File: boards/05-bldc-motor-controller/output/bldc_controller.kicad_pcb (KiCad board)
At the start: 2 copper layers, 80 x 100 mm, 55 parts, among them J1 Power Input, J2 Motor Output, J3 Hall Sensors, J4 SWD-6, Q1 IRLZ44N, Q2 IRLZ44N, Q3 IRLZ44N, Q4 IRLZ44N, Q5 IRLZ44N, Q6 IRLZ44N, U1 LM2596-5.0, U10 STM32G431K8Tx, U2 AMS1117-3.3, U3 DRV8301, Y1 8MHz

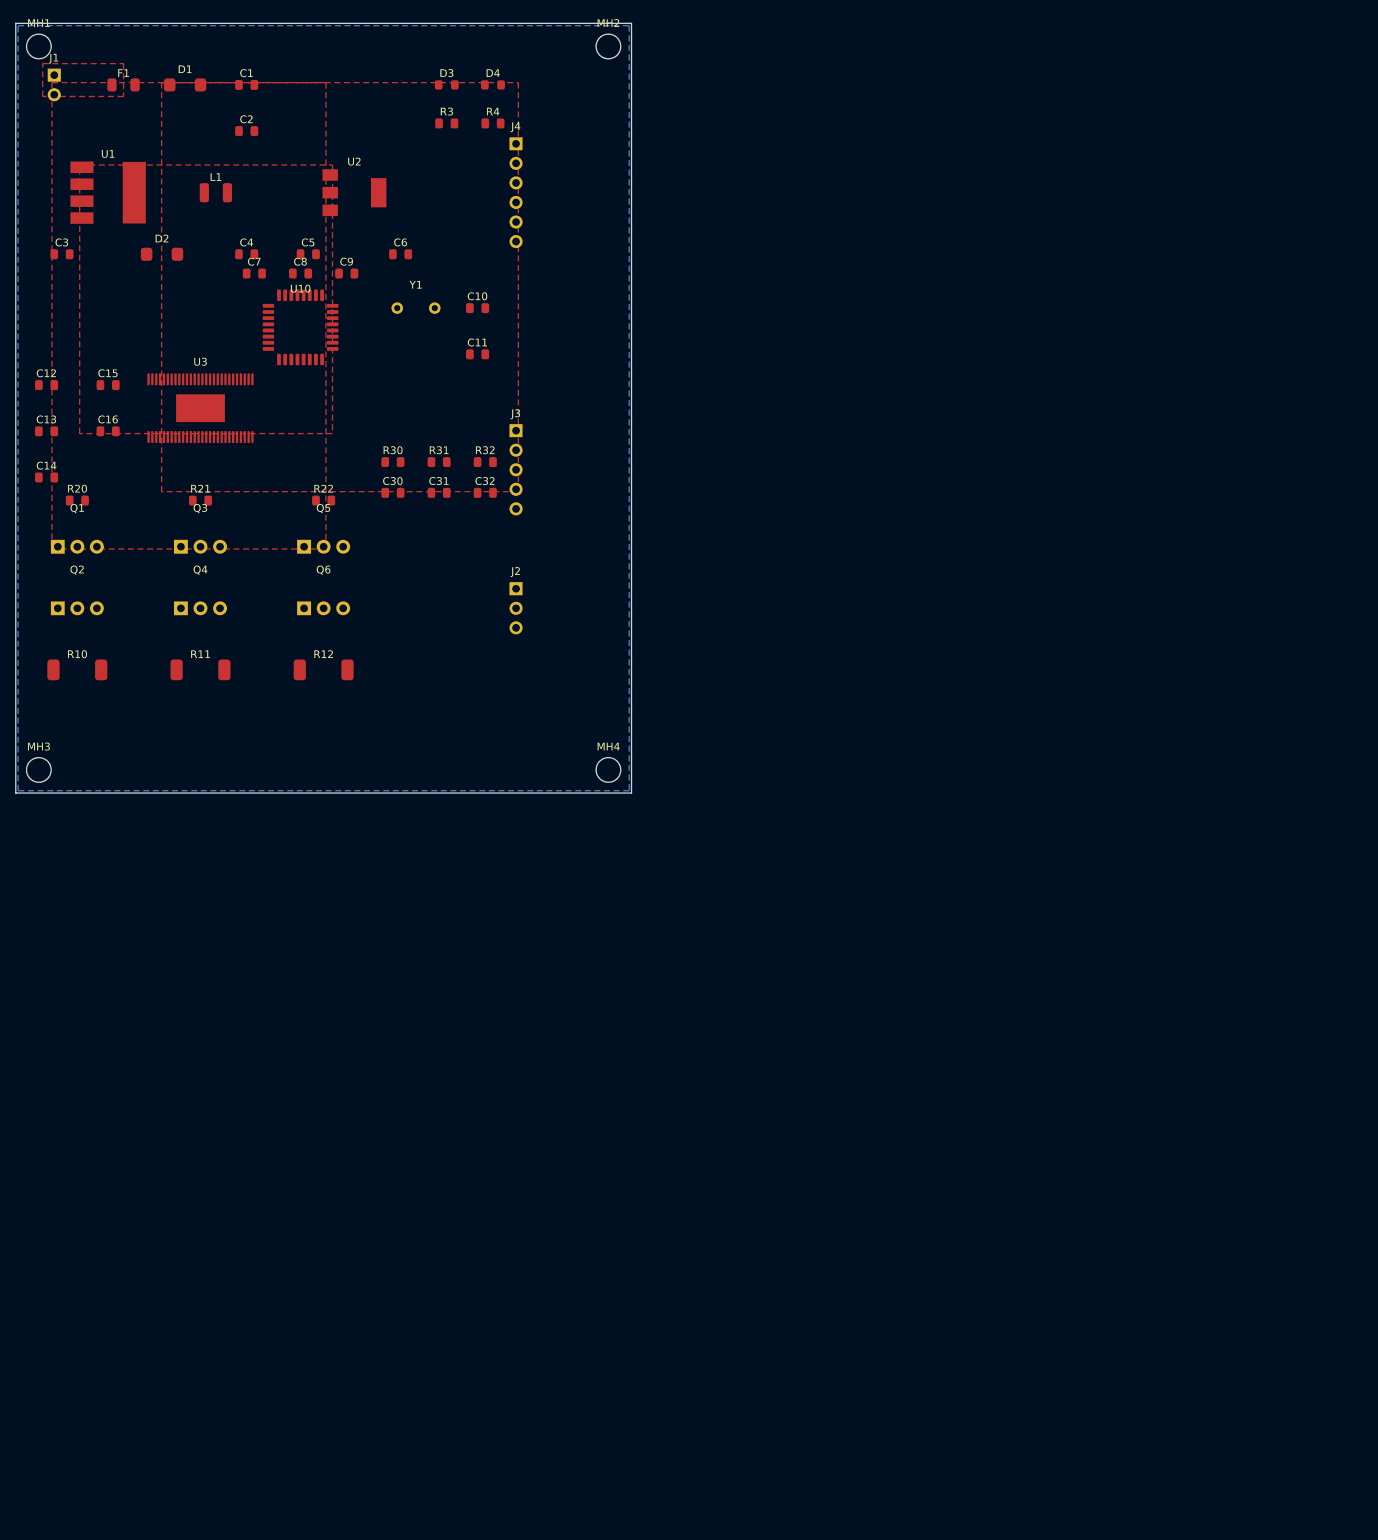
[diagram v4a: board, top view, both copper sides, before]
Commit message: fix(pcb): page-fit routed boards only; revert unrouted sources (refs #3714)
page_fit was applied to and committed for the UNROUTED board sources too.
Because the autorouter is absolute-grid-position-dependent, translating the
unrouted boards changed routing outcomes and turned CI red on three jobs:
- Test: board-02 re-route produced a platform-specific segment count.
- Diff-Pair (06) / Match-Group (07): re-routing the moved unrouted boards
  fractured plane nets under the copper-union pour audit (#3509/#3617).

page_fit is a pure post-route translation, so it must touch the ROUTED
output only:
- Revert every unrouted boards/*/output/<name>.kicad_pcb to origin/main
  (byte-identical); keep the page-fitted *_routed.kicad_pcb (gallery/viewer).
- Revert tests/router/test_board02_manufacturable_baseline.py to main
  (unrouted board-02 unchanged -> reproduces main's result).
- Build hook: _run_step_page_fit now operates on the routed PCB only and
  skips cleanly when no routed output exists, instead of falling back to and
  persisting a page-fit unrouted PCB.

Retains the sound geometry fixes (translation-invariant
point_to_segment_distance, _format_coord_mm, diffpair +1e-6 window tolerance).

Co-Authored-By: Claude Opus 4.7 <noreply@anthropic.com>
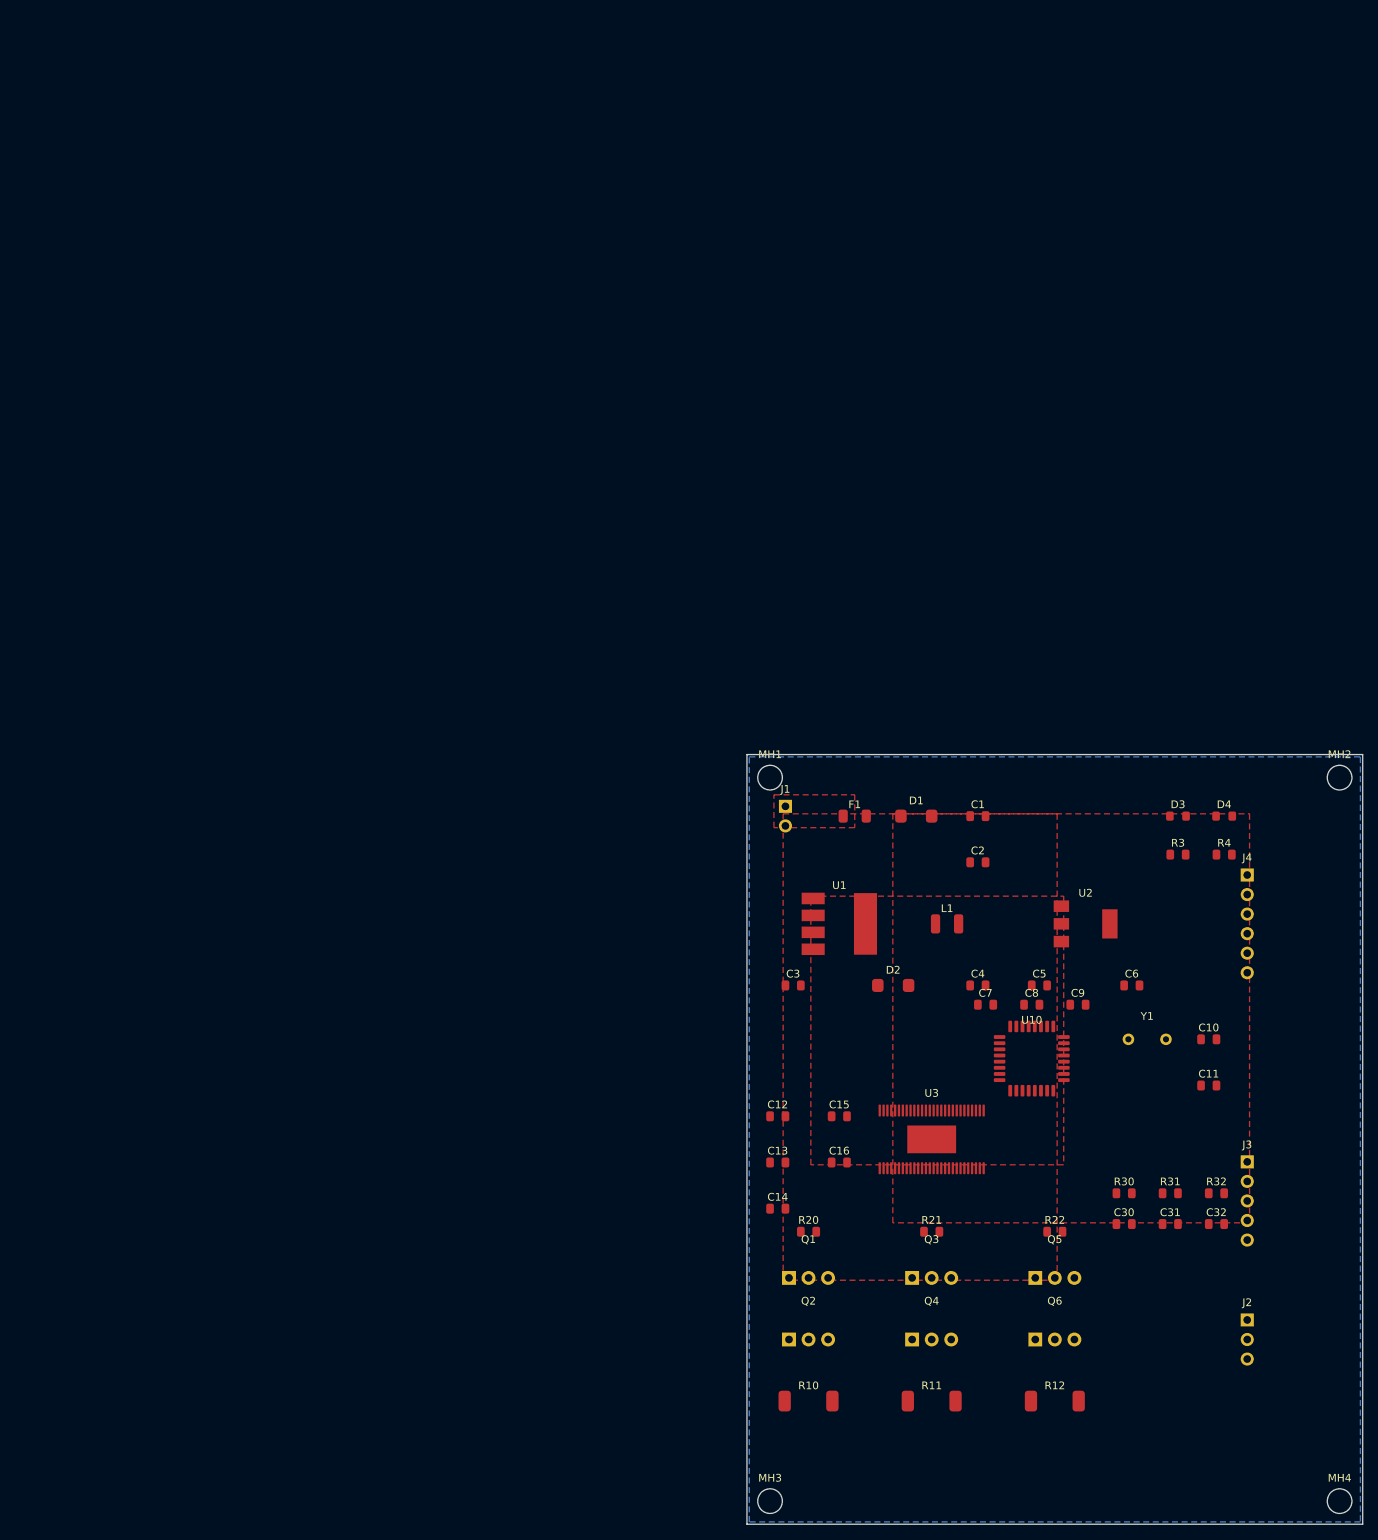
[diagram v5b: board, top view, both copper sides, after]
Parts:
- moved C1 134.4 mm to (130.0, 108.0)
- moved C10 134.4 mm to (160.0, 137.0)
- moved C11 134.4 mm to (160.0, 143.0)
- moved C12 134.4 mm to (104.0, 147.0)
- moved C13 134.4 mm to (104.0, 153.0)
- moved C14 134.4 mm to (104.0, 159.0)
- moved C15 134.4 mm to (112.0, 147.0)
- moved C16 134.4 mm to (112.0, 153.0)
- moved C2 134.4 mm to (130.0, 114.0)
- moved C3 134.4 mm to (106.0, 130.0)
- moved C30 134.4 mm to (149.0, 161.0)
- moved C31 134.4 mm to (155.0, 161.0)
- moved C32 134.4 mm to (161.0, 161.0)
- moved C4 134.4 mm to (130.0, 130.0)
- moved C5 134.4 mm to (138.0, 130.0)
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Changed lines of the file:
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@@
 (kicad_pcb
 	(version 20260206)
-	(paper "User" 90 110)
 	(generator "kicad-tools-demo")
 	(generator_version "10.0")
@@
 		(legacy_teardrops no)
 	)
+	(paper "A4")
 	(layers
 		(0 "F.Cu" signal)
@@
 	(net 52 "unconnected-(U10-PB5-Pad28)")
 	(gr_rect
-		(start 5 5)
-		(end 85 105)
+		(start 100.0 100.0)
+		(end 180.0 200.0)
 		(stroke
 			(width 0.1)
@@
 	(footprint "MountingHole:MountingHole_3.2mm_M3"
 		(layer "F.Cu")
-		(at 8 8)
+		(at 103.0 103.0)
 		(fp_text reference "MH1"
 			(at 0 -3)
@@
 	(footprint "MountingHole:MountingHole_3.2mm_M3"
 		(layer "F.Cu")
-		(at 82 8)
+		(at 177.0 103.0)
 		(fp_text reference "MH2"
 			(at 0 -3)
@@
 	(footprint "MountingHole:MountingHole_3.2mm_M3"
 		(layer "F.Cu")
-		(at 8 102)
+		(at 103.0 197.0)
 		(fp_text reference "MH3"
 			(at 0 -3)
@@
 	(footprint "MountingHole:MountingHole_3.2mm_M3"
 		(layer "F.Cu")
-		(at 82 102)
+		(at 177.0 197.0)
 		(fp_text reference "MH4"
 			(at 0 -3)
@@
 	(footprint "Connector_PinHeader_2.54mm:PinHeader_1x02_P2.54mm_Vertical"
 		(layer "F.Cu")
-		(at 10 13)
+		(at 105.0 108.0)
 		(fp_text reference "J1"
 			(at 0 -3.5)
@@
 	(footprint "Fuse:Fuse_1206_3216Metric"
 		(layer "F.Cu")
-		(at 19 13)
+		(at 114.0 108.0)
 		(fp_text reference "F1"
 			(at 0 -1.5)
@@
 	(footprint "Diode_SMD:D_SMA"
 		(layer "F.Cu")
-		(at 27 13)
+		(at 122.0 108.0)
 		(fp_text reference "D1"
 			(at 0 -2)
@@
 	(footprint "Capacitor_SMD:C_0805_2012Metric"
 		(layer "F.Cu")
-		(at 35 13)
+		(at 130.0 108.0)
 		(fp_text reference "C1"
 			(at 0 -1.5)
@@
 	(footprint "Capacitor_SMD:C_0805_2012Metric"
 		(layer "F.Cu")
-		(at 35 19)
+		(at 130.0 114.0)
 		(fp_text reference "C2"
 			(at 0 -1.5)
@@
 	(footprint "Package_TO_SOT_SMD:TO-263-5_TabPin3"
 		(layer "F.Cu")
-		(at 17 27)
+		(at 112.0 122.0)
 		(fp_text reference "U1"
 			(at 0 -5)
@@
 	(footprint "Inductor_SMD:L_1210_3225Metric"
 		(layer "F.Cu")
-		(at 31 27)
+		(at 126.0 122.0)
 		(fp_text reference "L1"
 			(at 0 -2)
@@
 	(footprint "Diode_SMD:D_SMA"
 		(layer "F.Cu")
-		(at 24 35)
+		(at 119.0 130.0)
 		(fp_text reference "D2"
 			(at 0 -2)
@@
 	(footprint "Capacitor_SMD:C_0805_2012Metric"
 		(layer "F.Cu")
-		(at 11 35)
+		(at 106.0 130.0)
 		(fp_text reference "C3"
 			(at 0 -1.5)
@@
 	(footprint "Capacitor_SMD:C_0805_2012Metric"
 		(layer "F.Cu")
-		(at 35 35)
+		(at 130.0 130.0)
 		(fp_text reference "C4"
 			(at 0 -1.5)
@@
 	(footprint "Package_TO_SOT_SMD:SOT-223-3_TabPin2"
 		(layer "F.Cu")
-		(at 49 27)
+		(at 144.0 122.0)
 		(fp_text reference "U2"
 			(at 0 -4)
@@
 	(footprint "Capacitor_SMD:C_0805_2012Metric"
 		(layer "F.Cu")
-		(at 43 35)
+		(at 138.0 130.0)
 		(fp_text reference "C5"
 			(at 0 -1.5)
@@
 	(footprint "Capacitor_SMD:C_0805_2012Metric"
 		(layer "F.Cu")
-		(at 55 35)
+		(at 150.0 130.0)
 		(fp_text reference "C6"
 			(at 0 -1.5)
@@
 	(footprint "Capacitor_SMD:C_0805_2012Metric"
 		(layer "F.Cu")
-		(at 36 37.5)
+		(at 131.0 132.5)
 		(fp_text reference "C7"
 			(at 0 -1.5)
@@
 	(footprint "Capacitor_SMD:C_0805_2012Metric"
 		(layer "F.Cu")
-		(at 42 37.5)
+		(at 137.0 132.5)
 		(fp_text reference "C8"
 			(at 0 -1.5)
@@
 	(footprint "Capacitor_SMD:C_0805_2012Metric"
 		(layer "F.Cu")
-		(at 48 37.5)
+		(at 143.0 132.5)
 		(fp_text reference "C9"
 			(at 0 -1.5)
@@
 	(footprint "Crystal:Crystal_HC49-4H_Vertical"
 		(layer "F.Cu")
-		(at 57 42)
+		(at 152.0 137.0)
 		(fp_text reference "Y1"
 			(at 0 -3)
@@
 	(footprint "Capacitor_SMD:C_0805_2012Metric"
 		(layer "F.Cu")
-		(at 65 42)
+		(at 160.0 137.0)
 		(fp_text reference "C10"
 			(at 0 -1.5)
@@
 	(footprint "Capacitor_SMD:C_0805_2012Metric"
 		(layer "F.Cu")
-		(at 65 48)
+		(at 160.0 143.0)
 		(fp_text reference "C11"
 			(at 0 -1.5)
@@
 	(footprint "Package_SO:HTSSOP-56-1EP_6.1x14mm_P0.5mm_EP3.61x6.35mm"
 		(layer "F.Cu")
-		(at 29 55)
+		(at 124.0 150.0)
 		(fp_text reference "U3"
 			(at 0 -6)
@@
 	(footprint "Capacitor_SMD:C_0805_2012Metric"
 		(layer "F.Cu")
-		(at 9 52)
+		(at 104.0 147.0)
 		(fp_text reference "C12"
 			(at 0 -1.5)
@@
 	(footprint "Capacitor_SMD:C_0805_2012Metric"
 		(layer "F.Cu")
-		(at 9 58)
+		(at 104.0 153.0)
 		(fp_text reference "C13"
 			(at 0 -1.5)
@@
 	(footprint "Capacitor_SMD:C_0805_2012Metric"
 		(layer "F.Cu")
-		(at 9 64)
+		(at 104.0 159.0)
 		(fp_text reference "C14"
 			(at 0 -1.5)
@@
 	(footprint "Capacitor_SMD:C_0805_2012Metric"
 		(layer "F.Cu")
-		(at 17 52)
+		(at 112.0 147.0)
 		(fp_text reference "C15"
 			(at 0 -1.5)
@@
 	(footprint "Capacitor_SMD:C_0805_2012Metric"
 		(layer "F.Cu")
-		(at 17 58)
+		(at 112.0 153.0)
 		(fp_text reference "C16"
 			(at 0 -1.5)
@@
 	(footprint "Package_QFP:LQFP-32_7x7mm_P0.8mm"
 		(layer "F.Cu")
-		(at 42 44.5)
+		(at 137.0 139.5)
 		(fp_text reference "U10"
 			(at 0 -5)
@@
 	(footprint "Package_TO_SOT_THT:TO-220-3_Vertical"
 		(layer "F.Cu")
-		(at 13 73)
+		(at 108.0 168.0)
 		(fp_text reference "Q1"
 			(at 0 -5)
@@
 	(footprint "Package_TO_SOT_THT:TO-220-3_Vertical"
 		(layer "F.Cu")
-		(at 13 81)
+		(at 108.0 176.0)
 		(fp_text reference "Q2"
 			(at 0 -5)
@@
 	(footprint "Package_TO_SOT_THT:TO-220-3_Vertical"
 		(layer "F.Cu")
-		(at 29 73)
+		(at 124.0 168.0)
 		(fp_text reference "Q3"
 			(at 0 -5)
@@
 	(footprint "Package_TO_SOT_THT:TO-220-3_Vertical"
 		(layer "F.Cu")
-		(at 29 81)
+		(at 124.0 176.0)
 		(fp_text reference "Q4"
 			(at 0 -5)
@@
 	(footprint "Package_TO_SOT_THT:TO-220-3_Vertical"
 		(layer "F.Cu")
-		(at 45 73)
+		(at 140.0 168.0)
 		(fp_text reference "Q5"
 			(at 0 -5)
@@
 	(footprint "Package_TO_SOT_THT:TO-220-3_Vertical"
 		(layer "F.Cu")
-		(at 45 81)
+		(at 140.0 176.0)
 		(fp_text reference "Q6"
 			(at 0 -5)
@@
 	(footprint "Resistor_SMD:R_2512_6332Metric"
 		(layer "F.Cu")
-		(at 13 89)
+		(at 108.0 184.0)
 		(fp_text reference "R10"
 			(at 0 -2)
@@
 	(footprint "Resistor_SMD:R_2512_6332Metric"
 		(layer "F.Cu")
-		(at 29 89)
+		(at 124.0 184.0)
 		(fp_text reference "R11"
 			(at 0 -2)
@@
 	(footprint "Resistor_SMD:R_2512_6332Metric"
 		(layer "F.Cu")
-		(at 45 89)
+		(at 140.0 184.0)
 		(fp_text reference "R12"
 			(at 0 -2)
@@
 	(footprint "Resistor_SMD:R_0805_2012Metric"
 		(layer "F.Cu")
-		(at 13 67)
+		(at 108.0 162.0)
 		(fp_text reference "R20"
 			(at 0 -1.5)
@@
 	(footprint "Resistor_SMD:R_0805_2012Metric"
 		(layer "F.Cu")
-		(at 29 67)
+		(at 124.0 162.0)
 		(fp_text reference "R21"
 			(at 0 -1.5)
@@
 	(footprint "Resistor_SMD:R_0805_2012Metric"
 		(layer "F.Cu")
-		(at 45 67)
+		(at 140.0 162.0)
 		(fp_text reference "R22"
 			(at 0 -1.5)
@@
 	(footprint "Connector_PinHeader_2.54mm:PinHeader_1x03_P2.54mm_Vertical"
 		(layer "F.Cu")
-		(at 70 81)
+		(at 165.0 176.0)
 		(fp_text reference "J2"
 			(at 0 -4.8)
@@
 	(footprint "Connector_PinHeader_2.54mm:PinHeader_1x05_P2.54mm_Vertical"
 		(layer "F.Cu")
-		(at 70 63)
+		(at 165.0 158.0)
 		(fp_text reference "J3"
 			(at 0 -7.3)
@@
 	(footprint "Connector_PinHeader_2.54mm:PinHeader_1x06_P2.54mm_Vertical"
 		(layer "F.Cu")
-		(at 70 27)
+		(at 165.0 122.0)
 		(fp_text reference "J4"
 			(at 0 -8.6)
@@
 	(footprint "Resistor_SMD:R_0805_2012Metric"
 		(layer "F.Cu")
-		(at 61 18)
+		(at 156.0 113.0)
 		(fp_text reference "R3"
 			(at 0 -1.5)
@@
 	(footprint "LED_SMD:LED_0805_2012Metric"
 		(layer "F.Cu")
-		(at 61 13)
+		(at 156.0 108.0)
 		(fp_text reference "D3"
 			(at 0 -1.5)
@@
 	(footprint "Resistor_SMD:R_0805_2012Metric"
 		(layer "F.Cu")
-		(at 67 18)
+		(at 162.0 113.0)
 		(fp_text reference "R4"
 			(at 0 -1.5)
@@
 	(footprint "LED_SMD:LED_0805_2012Metric"
 		(layer "F.Cu")
-		(at 67 13)
+		(at 162.0 108.0)
 		(fp_text reference "D4"
 			(at 0 -1.5)
@@
 	(footprint "Resistor_SMD:R_0805_2012Metric"
 		(layer "F.Cu")
-		(at 54 62)
+		(at 149.0 157.0)
 		(fp_text reference "R30"
 			(at 0 -1.5)
@@
 	(footprint "Resistor_SMD:R_0805_2012Metric"
 		(layer "F.Cu")
-		(at 60 62)
+		(at 155.0 157.0)
 		(fp_text reference "R31"
 			(at 0 -1.5)
@@
 	(footprint "Resistor_SMD:R_0805_2012Metric"
 		(layer "F.Cu")
-		(at 66 62)
+		(at 161.0 157.0)
 		(fp_text reference "R32"
 			(at 0 -1.5)
@@
 	(footprint "Capacitor_SMD:C_0805_2012Metric"
 		(layer "F.Cu")
-		(at 54 66)
+		(at 149.0 161.0)
 		(fp_text reference "C30"
 			(at 0 -1.5)
@@
 	(footprint "Capacitor_SMD:C_0805_2012Metric"
 		(layer "F.Cu")
-		(at 60 66)
+		(at 155.0 161.0)
 		(fp_text reference "C31"
 			(at 0 -1.5)
@@
 	(footprint "Capacitor_SMD:C_0805_2012Metric"
 		(layer "F.Cu")
-		(at 66 66)
+		(at 161.0 161.0)
 		(fp_text reference "C32"
 			(at 0 -1.5)
@@
 		(fill yes (thermal_gap 0.3) (thermal_bridge_width 0.4)
 		)
-		(polygon (pts (xy 5.3 5.3) (xy 84.7 5.3) (xy 84.7 104.7) (xy 5.3 104.7))
+		(polygon (pts (xy 100.3 100.3) (xy 179.7 100.3) (xy 179.7 199.7) (xy 100.3 199.7))
 		)
 	)
@@
 		(fill yes (thermal_gap 0.3) (thermal_bridge_width 0.4)
 		)
-		(polygon (pts (xy 9.7 12.7) (xy 45.3 12.7) (xy 45.3 73.3) (xy 9.7 73.3))
+		(polygon (pts (xy 104.7 107.7) (xy 140.3 107.7) (xy 140.3 168.3) (xy 104.7 168.3))
 		)
 	)
@@
 		(fill yes (thermal_gap 0.3) (thermal_bridge_width 0.4)
 		)
-		(polygon (pts (xy 13.3 23.4) (xy 46.15 23.4) (xy 46.15 58.3) (xy 13.3 58.3))
+		(polygon (pts (xy 108.3 118.4) (xy 141.15 118.4) (xy 141.15 153.3) (xy 108.3 153.3))
 		)
 	)
@@
 		(fill yes (thermal_gap 0.3) (thermal_bridge_width 0.4)
 		)
-		(polygon (pts (xy 23.95 12.7) (xy 70.3 12.7) (xy 70.3 65.84) (xy 23.95 65.84))
+		(polygon (pts (xy 118.95 107.7) (xy 165.3 107.7) (xy 165.3 160.84) (xy 118.95 160.84))
 		)
 	)
@@
 		(fill yes (thermal_gap 0.3) (thermal_bridge_width 0.4)
 		)
-		(polygon (pts (xy 8.5 10.23) (xy 19 10.23) (xy 19 14.5) (xy 8.5 14.5))
-		)
-	)
+		(polygon (pts (xy 103.5 105.23) (xy 114 105.23) (xy 114 109.5) (xy 103.5 109.5))
+		)
+	)
